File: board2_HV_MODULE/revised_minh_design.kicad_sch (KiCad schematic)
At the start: 13 parts, among them J1 Conn_01x07_Male, U1 LM7805_TO220, U2 NE5532, U3 CB101

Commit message: -
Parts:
- added R5, R7: 2K, Resistor_THT:R_Axial_DIN0309_L9.0mm_D3.2mm_P15.24mm_Horizontal, symbol Device:R
- added R6, R8: 1.1K, Resistor_THT:R_Axial_DIN0309_L9.0mm_D3.2mm_P15.24mm_Horizontal, symbol Device:R
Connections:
- net Earth: now also R6.1, R8.1
- net IMON: now also R7.2; no longer J1.5 (Pin_5)
- net VMON: now also R5.2; no longer J1.4 (Pin_4)
- new net IMON_3V3: J1.5 (Pin_5), R7.1, R8.2
- new net VMON_3V3: J1.4 (Pin_4), R5.1, R6.2

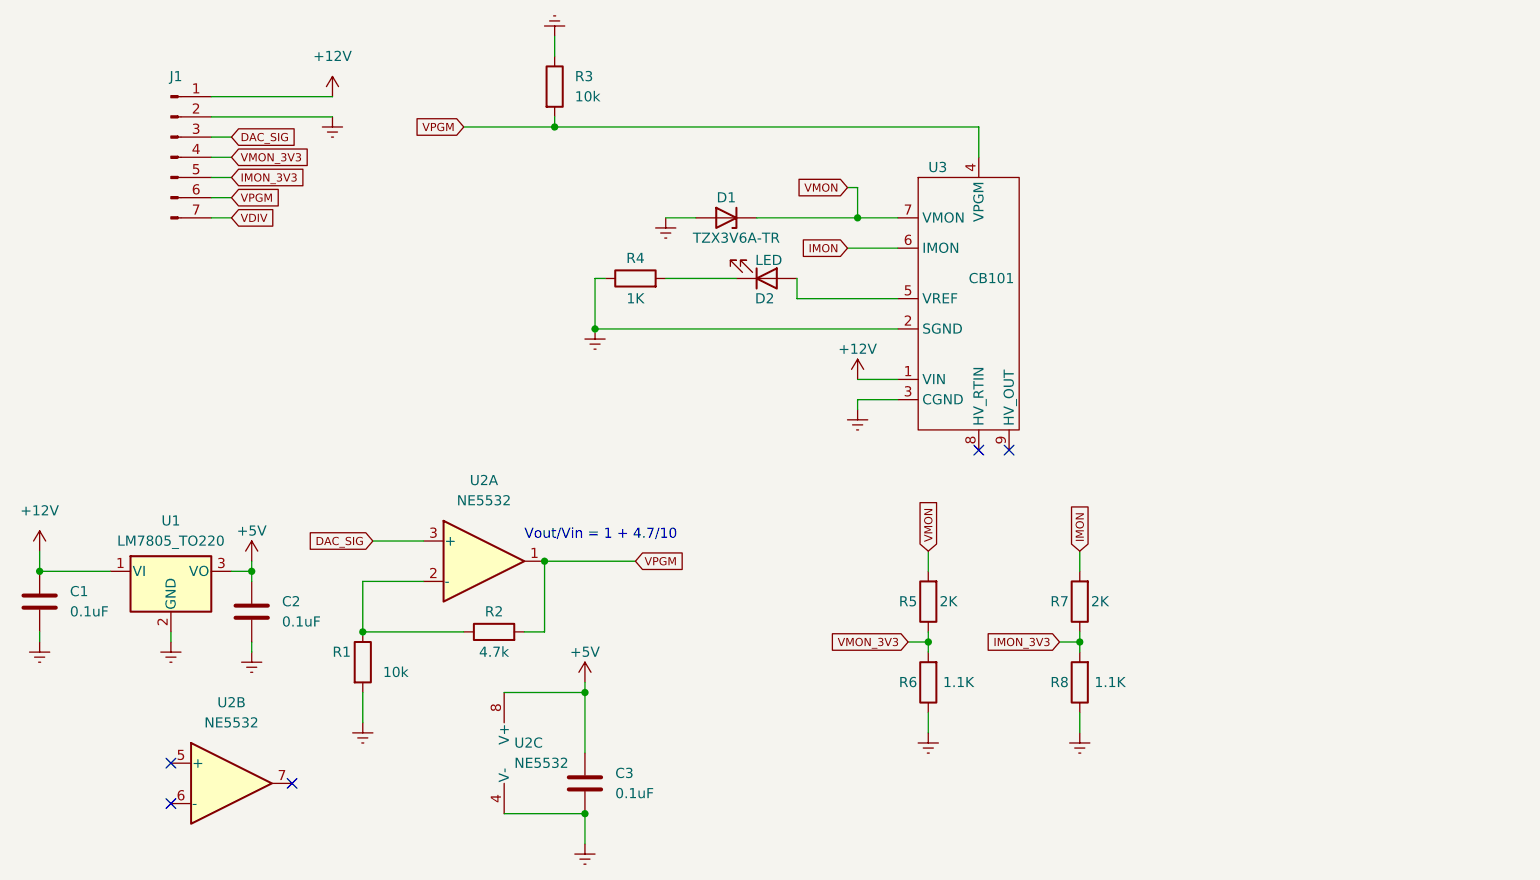
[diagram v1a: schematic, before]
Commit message: HV Module routed, some footprint changes
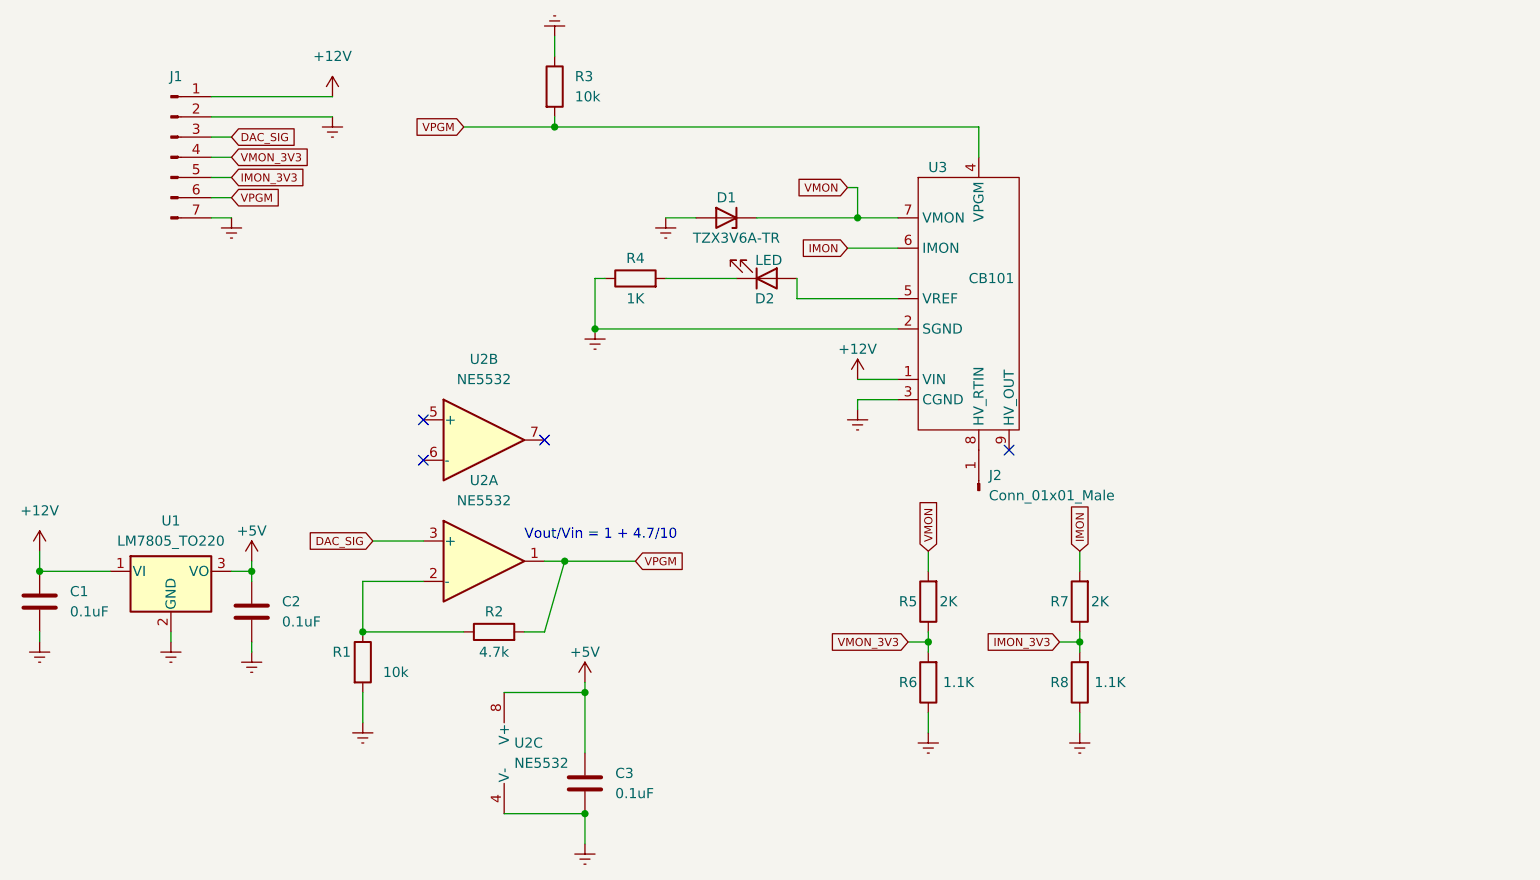
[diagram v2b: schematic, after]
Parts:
- added J2: Conn_01x01_Male, Connector_Wire:SolderWire-0.75sqmm_1x01_D1.25mm_OD2.3mm_Relief, symbol Connector:Conn_01x01_Male
- R1, R2, R3, R4, R5, R6, R7, R8: footprint Resistor_THT:R_Axial_DIN0309_L9.0mm_D3.2mm_P15.24mm_Horizontal -> Resistor_THT:R_Axial_DIN0207_L6.3mm_D2.5mm_P10.16mm_Horizontal
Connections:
- net VDIV is gone; now on net Earth: J1.7 (Pin_7)
- net at U3.8 (HV_RTIN): now also J2.1 (Pin_1)
- no-connect marks 5 -> 4
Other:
- moved on the sheet: U2B

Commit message: JLCPB Submission. Name added, connectors changed to double layer
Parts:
- R2: footprint Resistor_THT:R_Axial_DIN0207_L6.3mm_D2.5mm_P10.16mm_Horizontal -> Resistor_THT:R_Axial_DIN0207_L6.3mm_D2.5mm_P7.62mm_Horizontal
- R5: footprint Resistor_THT:R_Axial_DIN0207_L6.3mm_D2.5mm_P10.16mm_Horizontal -> Resistor_THT:R_Axial_DIN0207_L6.3mm_D2.5mm_P15.24mm_Horizontal
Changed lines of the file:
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@@
     (property "Reference" "R2" (id 0) (at 82.55 92.71 90))
     (property "Value" "4.7k" (id 1) (at 82.55 97.79 90))
-    (property "Footprint" "Resistor_THT:R_Axial_DIN0207_L6.3mm_D2.5mm_P10.16mm_Horizontal" (id 2) (at 82.55 97.028 90)
+    (property "Footprint" "Resistor_THT:R_Axial_DIN0207_L6.3mm_D2.5mm_P7.62mm_Horizontal" (id 2) (at 82.55 97.028 90)
       (effects (font (size 1.27 1.27)) hide)
     )
@@
     (property "Reference" "R5" (id 0) (at 134.62 91.44 0))
     (property "Value" "2K" (id 1) (at 139.7 91.44 0))
-    (property "Footprint" "Resistor_THT:R_Axial_DIN0207_L6.3mm_D2.5mm_P10.16mm_Horizontal" (id 2) (at 138.938 91.44 90)
+    (property "Footprint" "Resistor_THT:R_Axial_DIN0207_L6.3mm_D2.5mm_P15.24mm_Horizontal" (id 2) (at 138.938 91.44 90)
       (effects (font (size 1.27 1.27)) hide)
     )
@@
     )
     (path "/90448ba8-5502-4df1-8c21-bd3fac98bab5"
-      (reference "R2") (unit 1) (value "4.7k") (footprint "Resistor_THT:R_Axial_DIN0207_L6.3mm_D2.5mm_P10.16mm_Horizontal")
+      (reference "R2") (unit 1) (value "4.7k") (footprint "Resistor_THT:R_Axial_DIN0207_L6.3mm_D2.5mm_P7.62mm_Horizontal")
     )
     (path "/98700803-79a8-4ec2-bc5e-3326e28aa2cc"
@@
     )
     (path "/a4e2fe62-1543-4398-8850-30b5933e3401"
-      (reference "R5") (unit 1) (value "2K") (footprint "Resistor_THT:R_Axial_DIN0207_L6.3mm_D2.5mm_P10.16mm_Horizontal")
+      (reference "R5") (unit 1) (value "2K") (footprint "Resistor_THT:R_Axial_DIN0207_L6.3mm_D2.5mm_P15.24mm_Horizontal")
     )
     (path "/494f5535-0d2a-461b-8b71-f86f3a6a73ff"

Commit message: exported STEP file. Minor changes to schematics for better documentations
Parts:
- J2: now left out of the parts list
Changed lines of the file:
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@@
   )
   (symbol (lib_id "Connector:Conn_01x01_Male") (at 143.51 77.47 90) (unit 1)
-    (in_bom yes) (on_board yes) (fields_autoplaced)
+    (in_bom no) (on_board yes) (fields_autoplaced)
     (property "Reference" "J2" (id 0) (at 144.78 75.5649 90)
       (effects (font (size 1.27 1.27)) (justify right))

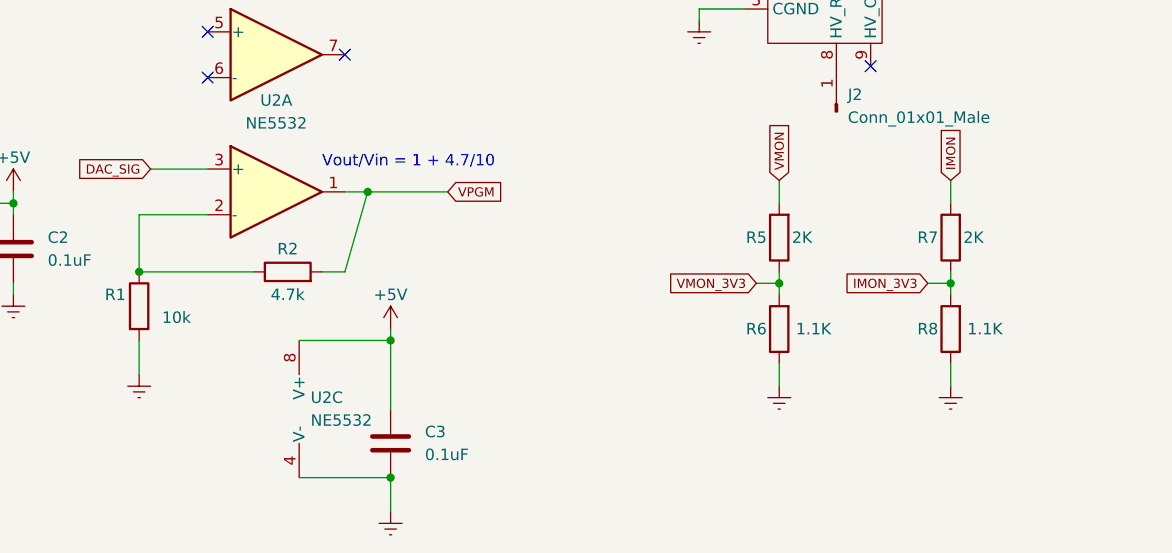
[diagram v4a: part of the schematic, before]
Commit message: Fixed PI PO, DAC port ordering, MDAT Pin, clock connection
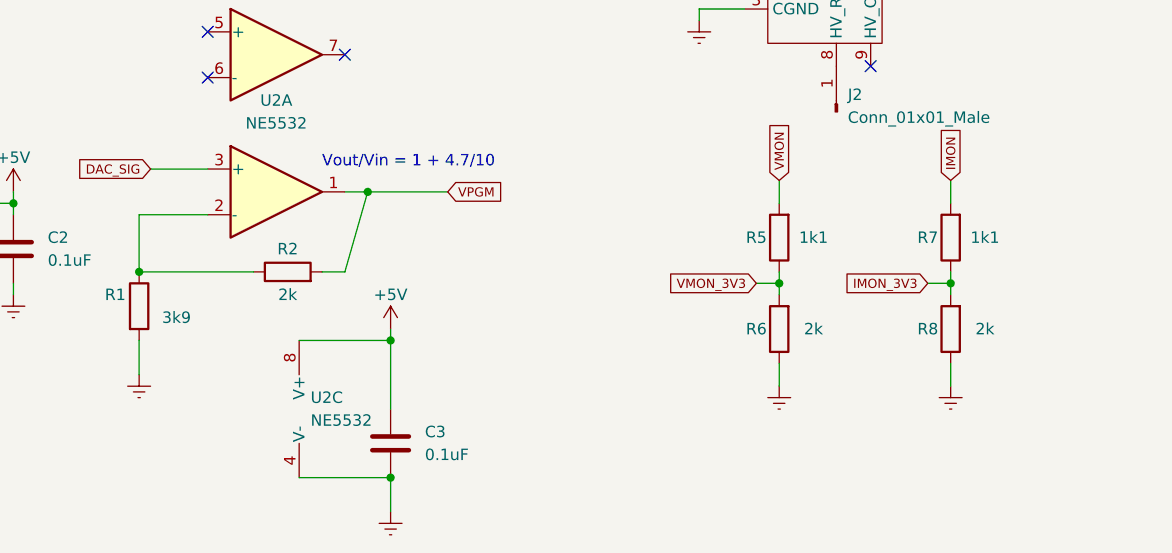
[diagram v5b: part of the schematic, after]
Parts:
- R1: value 10k -> 3k9
- R2: value 4.7k -> 2k
- R5, R7: value 2K -> 1k1
- R6, R8: value 1.1K -> 2k
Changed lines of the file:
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@@
     (in_bom yes) (on_board yes)
     (property "Reference" "R6" (id 0) (at 134.62 101.6 0))
-    (property "Value" "1.1K" (id 1) (at 140.97 101.6 0))
+    (property "Value" "2k" (id 1) (at 140.97 101.6 0))
     (property "Footprint" "Resistor_THT:R_Axial_DIN0207_L6.3mm_D2.5mm_P10.16mm_Horizontal" (id 2) (at 138.938 101.6 90)
       (effects (font (size 1.27 1.27)) hide)
@@
     (in_bom yes) (on_board yes)
     (property "Reference" "R2" (id 0) (at 82.55 92.71 90))
-    (property "Value" "4.7k" (id 1) (at 82.55 97.79 90))
+    (property "Value" "2k" (id 1) (at 82.55 97.79 90))
     (property "Footprint" "Resistor_THT:R_Axial_DIN0207_L6.3mm_D2.5mm_P7.62mm_Horizontal" (id 2) (at 82.55 97.028 90)
       (effects (font (size 1.27 1.27)) hide)
@@
     (in_bom yes) (on_board yes)
     (property "Reference" "R8" (id 0) (at 153.67 101.6 0))
-    (property "Value" "1.1K" (id 1) (at 160.02 101.6 0))
+    (property "Value" "2k" (id 1) (at 160.02 101.6 0))
     (property "Footprint" "Resistor_THT:R_Axial_DIN0207_L6.3mm_D2.5mm_P10.16mm_Horizontal" (id 2) (at 157.988 101.6 90)
       (effects (font (size 1.27 1.27)) hide)
@@
     (in_bom yes) (on_board yes)
     (property "Reference" "R7" (id 0) (at 153.67 91.44 0))
-    (property "Value" "2K" (id 1) (at 158.75 91.44 0))
+    (property "Value" "1k1" (id 1) (at 160.02 91.44 0))
     (property "Footprint" "Resistor_THT:R_Axial_DIN0207_L6.3mm_D2.5mm_P10.16mm_Horizontal" (id 2) (at 157.988 91.44 90)
       (effects (font (size 1.27 1.27)) hide)
@@
     (in_bom yes) (on_board yes)
     (property "Reference" "R5" (id 0) (at 134.62 91.44 0))
-    (property "Value" "2K" (id 1) (at 139.7 91.44 0))
+    (property "Value" "1k1" (id 1) (at 140.97 91.44 0))
     (property "Footprint" "Resistor_THT:R_Axial_DIN0207_L6.3mm_D2.5mm_P15.24mm_Horizontal" (id 2) (at 138.938 91.44 90)
       (effects (font (size 1.27 1.27)) hide)
@@
       (effects (font (size 1.27 1.27)) (justify left))
     )
-    (property "Value" "10k" (id 1) (at 68.58 100.3299 0)
+    (property "Value" "3k9" (id 1) (at 68.58 100.3299 0)
       (effects (font (size 1.27 1.27)) (justify left))
     )
@@
     )
     (path "/b29a57d3-9503-4ca1-a1b1-94063a0f28ae"
-      (reference "R1") (unit 1) (value "10k") (footprint "Resistor_THT:R_Axial_DIN0207_L6.3mm_D2.5mm_P10.16mm_Horizontal")
+      (reference "R1") (unit 1) (value "3k9") (footprint "Resistor_THT:R_Axial_DIN0207_L6.3mm_D2.5mm_P10.16mm_Horizontal")
     )
     (path "/90448ba8-5502-4df1-8c21-bd3fac98bab5"
-      (reference "R2") (unit 1) (value "4.7k") (footprint "Resistor_THT:R_Axial_DIN0207_L6.3mm_D2.5mm_P7.62mm_Horizontal")
+      (reference "R2") (unit 1) (value "2k") (footprint "Resistor_THT:R_Axial_DIN0207_L6.3mm_D2.5mm_P7.62mm_Horizontal")
     )
     (path "/98700803-79a8-4ec2-bc5e-3326e28aa2cc"
@@
     )
     (path "/a4e2fe62-1543-4398-8850-30b5933e3401"
-      (reference "R5") (unit 1) (value "2K") (footprint "Resistor_THT:R_Axial_DIN0207_L6.3mm_D2.5mm_P15.24mm_Horizontal")
+      (reference "R5") (unit 1) (value "1k1") (footprint "Resistor_THT:R_Axial_DIN0207_L6.3mm_D2.5mm_P15.24mm_Horizontal")
     )
     (path "/494f5535-0d2a-461b-8b71-f86f3a6a73ff"
-      (reference "R6") (unit 1) (value "1.1K") (footprint "Resistor_THT:R_Axial_DIN0207_L6.3mm_D2.5mm_P10.16mm_Horizontal")
+      (reference "R6") (unit 1) (value "2k") (footprint "Resistor_THT:R_Axial_DIN0207_L6.3mm_D2.5mm_P10.16mm_Horizontal")
     )
     (path "/a2dea781-9bc1-4d50-828e-caa9d3943e1c"
-      (reference "R7") (unit 1) (value "2K") (footprint "Resistor_THT:R_Axial_DIN0207_L6.3mm_D2.5mm_P10.16mm_Horizontal")
+      (reference "R7") (unit 1) (value "1k1") (footprint "Resistor_THT:R_Axial_DIN0207_L6.3mm_D2.5mm_P10.16mm_Horizontal")
     )
     (path "/93d2ccfb-9bbb-4ea8-8868-a325feda37a0"
-      (reference "R8") (unit 1) (value "1.1K") (footprint "Resistor_THT:R_Axial_DIN0207_L6.3mm_D2.5mm_P10.16mm_Horizontal")
+      (reference "R8") (unit 1) (value "2k") (footprint "Resistor_THT:R_Axial_DIN0207_L6.3mm_D2.5mm_P10.16mm_Horizontal")
     )
     (path "/34ad081a-2df0-4615-aad1-bf529e317b2a"
